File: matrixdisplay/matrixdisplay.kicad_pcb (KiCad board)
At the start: 2 copper layers, 73 x 31 mm, 93 parts, among them J1 FILAS, J2 COLUMNAS, J3 SWD, J4 USART, J5 FILAS, J6 COL, SW1 BT1, SW2 BT2, SW2 P_ON, U1 STM32F051K8Ux

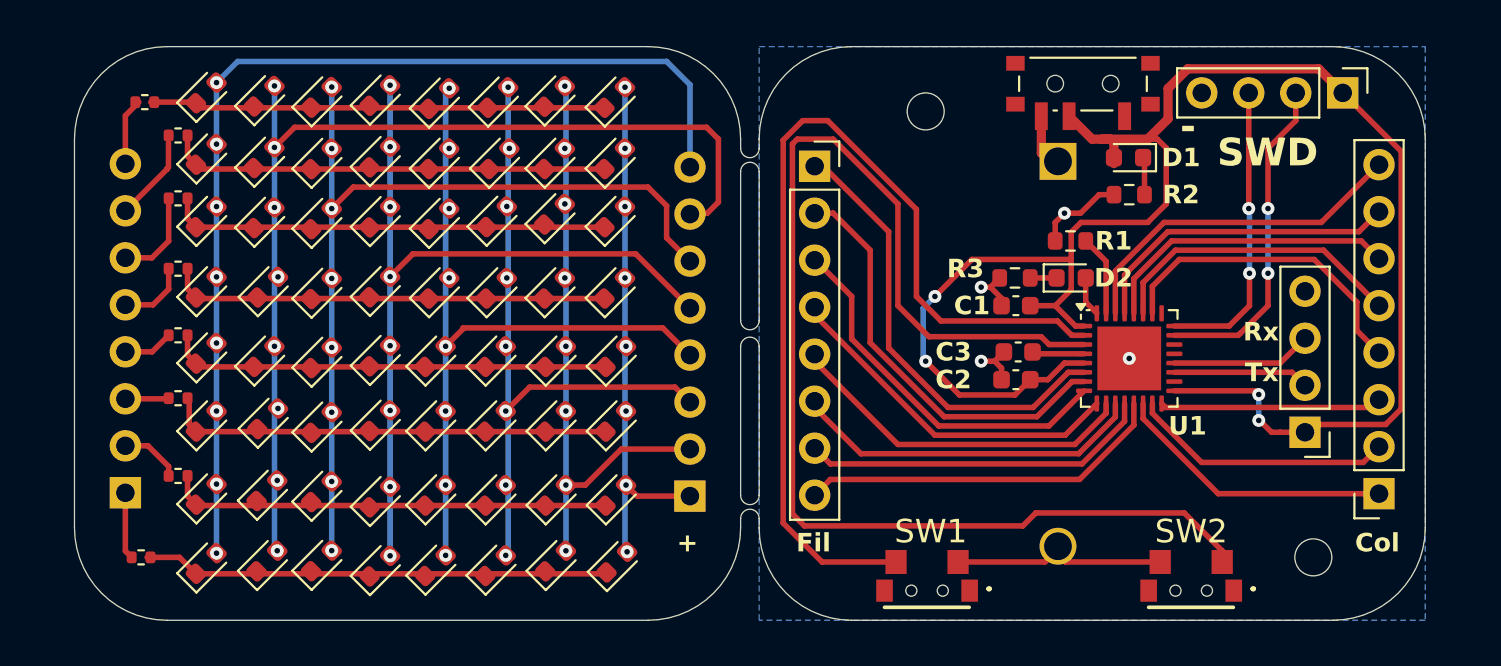
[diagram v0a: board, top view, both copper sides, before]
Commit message: feat(brd): reroute for CR2450
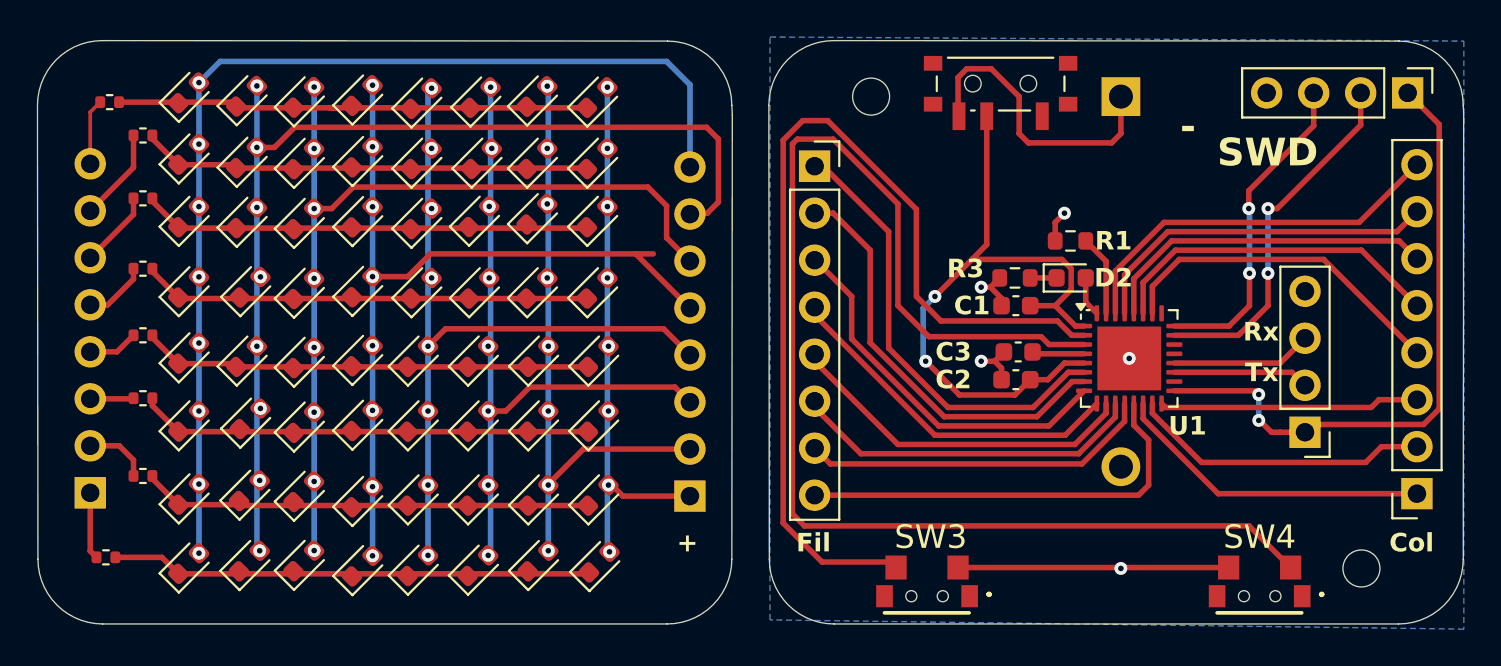
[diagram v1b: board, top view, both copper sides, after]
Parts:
- removed D1: LED, LED_SMD:LED_0603_1608Metric
- removed R2: 220, Resistor_SMD:R_0603_1608Metric
- BT1: value CR2032 -> CR2450; footprint Battery:BatteryHolder_MYOUNG_BS-07-A1BJ001_CR2032 -> Battery:BatteryHolder_ComfortableElectronic_CH273-2450_1x2450
- moved BT1 4.88 mm to (173.0, 77.5)
- moved SW2 4.45 mm to (166.5, 77.1)
- moved SW4 3.71 mm to (180.5, 104.5)
- moved J3 3.51 mm to (188.5, 77.3)
- moved H1 3.06 mm to (159.5, 77.5)
- moved H2 2.67 mm to (186.0, 103.0)
- moved J2 2.05 mm to (189.0, 99.0)
- moved J6 1.90 mm to (117.3, 98.9)
- moved R11 1.90 mm to (118.3, 77.8)
- moved R10 1.90 mm to (120.2, 79.6)
- moved R4 1.90 mm to (118.2, 102.4)
- moved R5 1.90 mm to (120.2, 98.0)
- moved R6 1.90 mm to (120.2, 93.8)
- moved R7 1.90 mm to (120.2, 90.4)
- moved R8 1.90 mm to (120.2, 86.8)
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- renumbered SW1 to SW3, SW2 to SW4
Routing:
- net +3.3V: track 93.4 -> 70.4 mm
- net Net-(BT1-+): track 3.05 -> 16.1 mm
- net Net-(J1-Pin_8): track 20.0 -> 23.0 mm
- net Net-(U1-PF1): track 68.9 -> 71.8 mm
- net Net-(J2-Pin_5): track 16.4 -> 18.4 mm
- net Net-(J2-Pin_3): track 12.0 -> 14.1 mm
- net Net-(J2-Pin_1): track 15.2 -> 17.3 mm
- net Net-(J2-Pin_8): track 18.9 -> 21.0 mm
- net Net-(J2-Pin_7): track 17.2 -> 19.3 mm
- net Net-(J2-Pin_6): track 16.4 -> 18.4 mm
- net Net-(J2-Pin_2): track 14.2 -> 16.3 mm
- net Net-(D1-K): track 2.03 -> 0.00 mm
- net Net-(D27-A): track 43.6 -> 45.5 mm
- net Net-(J3-Pin_2): track 17.8 -> 19.6 mm
- net Net-(J3-Pin_3): track 16.0 -> 17.5 mm
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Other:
- board size 73 x 31 mm -> 77.1 x 31.5 mm

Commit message: Fix (brd): DRC errors
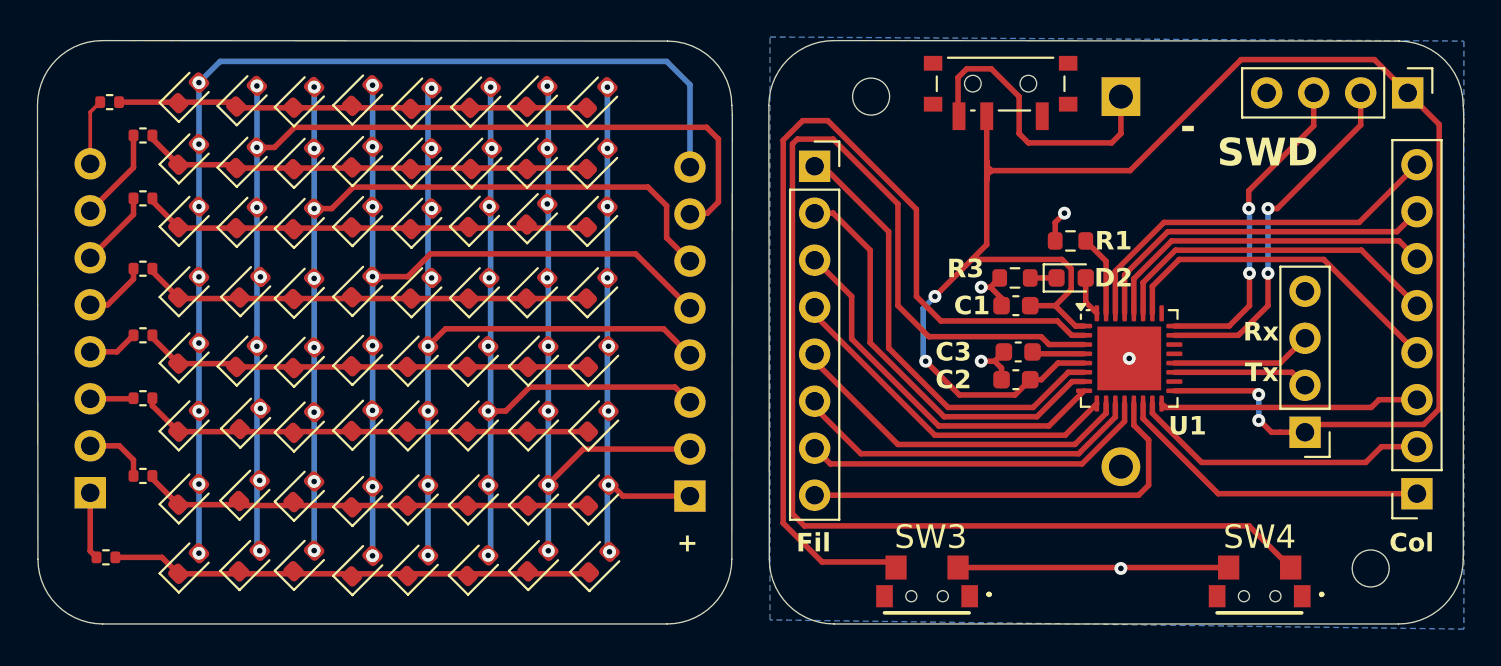
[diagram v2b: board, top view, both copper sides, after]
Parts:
- moved H2 0.50 mm to (186.5, 103.0)
- renumbered BT1 to +
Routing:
- net +3.3V: track 70.4 -> 97.6 mm
- net Net-(D27-A): track 45.5 -> 44.5 mm
- net GND: track 22.0 -> 21.4 mm
- net Net-(D11-K): track 25.9 -> 25.4 mm
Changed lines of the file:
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@@
 	(footprint "MountingHole:MountingHole_2mm"
 		(layer "F.Cu")
-		(at 186 103)
+		(at 186.5 103)
 		(descr "Mounting Hole 2mm, no annular")
 		(tags "mounting hole 2mm no annular")
@@
 		(descr "Comfortable Electronic CR2450 battery holder, http://www.comf.com.tw/ProductDetail.asp?no=148")
 		(tags "Comfortable Electronic CR2450")
-		(property "Reference" "BT1"
+		(property "Reference" "+"
 			(at 0.1 6.62 90)
 			(layer "B.SilkS")
@@
 				(font
 					(size 1 1)
-					(thickness 0.15)
+					(thickness 0.2)
+					(bold yes)
 				)
 				(justify mirror)
@@
 	)
 	(gr_text "ArcMaker\n${VERSION}"
-		(at 161.5 82.5 0)
+		(at 184.25 82 0)
 		(layer "B.SilkS")
 		(effects
 			(font
-				(size 0.75 1)
-				(thickness 0.1875)
+				(size 1 1)
+				(thickness 0.2)
 				(bold yes)
 			)
@@
 	)
 	(segment
-		(start 178.976 102.857521)
-		(end 178.976 102.65)
-		(width 0.3)
-		(layer "F.Cu")
-		(net 1)
-	)
-	(segment
 		(start 165.95 87.8)
 		(end 166.45 87.3)
@@
 	)
 	(segment
-		(start 178.682521 103.151)
-		(end 178.976 102.857521)
-		(width 0.3)
-		(layer "F.Cu")
-		(net 1)
-	)
-	(segment
 		(start 169.45 85.3)
 		(end 169.45 84.3)
@@
 	)
 	(segment
+		(start 165.75 81.25)
+		(end 166 81.5)
+		(width 0.3)
+		(layer "F.Cu")
+		(net 3)
+	)
+	(segment
 		(start 165.75 78.56)
-		(end 165.75 85.5)
+		(end 165.75 81)
 		(width 0.3)
 		(layer "F.Cu")
@@
 	)
 	(segment
-		(start 175.8875 93.4)
-		(end 180.25 93.4)
+		(start 180.25 93.4)
+		(end 180.45 93.6)
 		(width 0.3)
 		(layer "F.Cu")
@@
 	)
 	(segment
-		(start 180.25 93.4)
-		(end 180.45 93.6)
+		(start 165.75 81)
+		(end 165.75 81.5)
 		(width 0.3)
 		(layer "F.Cu")
@@
 	)
 	(segment
+		(start 165.75 81.75)
+		(end 166 81.5)
+		(width 0.3)
+		(layer "F.Cu")
+		(net 3)
+	)
+	(segment
 		(start 164.95 86.3)
 		(end 165.75 85.5)
@@
 	)
 	(segment
-		(start 169.05 92.8)
-		(end 169.95 91.9)
+		(start 179.5 75.5)
+		(end 173.5 81.5)
+		(width 0.3)
+		(layer "F.Cu")
+		(net 3)
+	)
+	(segment
+		(start 173.5 81.5)
+		(end 166 81.5)
 		(width 0.3)
 		(layer "F.Cu")
@@
 	)
 	(segment
-		(start 169.95 91.9)
-		(end 171.0125 91.9)
+		(start 188.5 77.3)
+		(end 186.7 75.5)
 		(width 0.3)
 		(layer "F.Cu")
@@
 	)
 	(segment
+		(start 165.75 82)
+		(end 165.75 81.75)
+		(width 0.3)
+		(layer "F.Cu")
+		(net 3)
+	)
+	(segment
+		(start 169.6 91.9)
+		(end 168.7 92.8)
+		(width 0.3)
+		(layer "F.Cu")
+		(net 3)
+	)
+	(segment
 		(start 162.95 88.3)
 		(end 164.95 86.3)
@@
 	)
 	(segment
+		(start 165.75 82)
+		(end 165.75 85.5)
+		(width 0.3)
+		(layer "F.Cu")
+		(net 3)
+	)
+	(segment
 		(start 180.45 94.95)
 		(end 181.14 95.64)
@@
 	)
 	(segment
+		(start 171.0125 91.9)
+		(end 169.6 91.9)
+		(width 0.3)
+		(layer "F.Cu")
+		(net 3)
+	)
+	(segment
+		(start 165.75 81.5)
+		(end 165.75 82)
+		(width 0.3)
+		(layer "F.Cu")
+		(net 3)
+	)
+	(segment
 		(start 190.201 79.001)
 		(end 188.5 77.3)
@@
 	)
 	(segment
+		(start 168.7 92.8)
+		(end 168.1 92.8)
+		(width 0.3)
+		(layer "F.Cu")
+		(net 3)
+	)
+	(segment
 		(start 181.61 95.64)
 		(end 182.95 95.64)
@@
 	)
 	(segment
+		(start 175.8875 93.4)
+		(end 180.25 93.4)
+		(width 0.3)
+		(layer "F.Cu")
+		(net 3)
+	)
+	(segment
+		(start 186.7 75.5)
+		(end 179.5 75.5)
+		(width 0.3)
+		(layer "F.Cu")
+		(net 3)
+	)
+	(segment
 		(start 167.275 93.625)
 		(end 164.275 93.625)
@@
 	)
 	(segment
+		(start 166 81.5)
+		(end 165.75 81.5)
+		(width 0.3)
+		(layer "F.Cu")
+		(net 3)
+	)
+	(segment
 		(start 190.201 94.377471)
 		(end 190.201 79.001)
@@
 	)
 	(segment
-		(start 168.1 92.8)
-		(end 169.05 92.8)
+		(start 165.75 81)
+		(end 165.75 81.25)
 		(width 0.3)
 		(layer "F.Cu")
@@
 	)
 	(segment
-		(start 180.45 93.6)
-		(end 180.45 95)
-		(width 0.3)
-		(layer "B.Cu")
-		(net 3)
-	)
-	(segment
 		(start 162.316835 88.933165)
 		(end 162.95 88.3)
@@
 	)
 	(segment
+		(start 180.45 95)
+		(end 180.45 93.6)
+		(width 0.3)
+		(layer "B.Cu")
+		(net 3)
+	)
+	(segment
 		(start 168.225 91.3)
 		(end 168.325 91.4)
@@
 	)
 	(segment
-		(start 171.1 88.6125)
-		(end 171.7 89.2125)
+		(start 171.1 87.3)
+		(end 171.1 88.6125)
 		(width 0.3)
 		(layer "F.Cu")
@@
 	)
 	(segment
-		(start 171.1 87.3)
-		(end 171.1 88.6125)
+		(start 171.1 88.6125)
+		(end 171.7 89.2125)
 		(width 0.3)
 		(layer "F.Cu")
@@
 	)
 	(segment
-		(start 130.188153 78.096847)
-		(end 130.6975 78.096847)
-		(width 0.3)
-		(layer "F.Cu")
-		(net 34)
-	)
-	(segment
 		(start 120.66 79.778694)
 		(end 122.063153 81.181847)
@@
 	)
 	(segment
-		(start 132.5575 87.23)
-		(end 134.4575 87.23)
+		(start 146.780652 86)
+		(end 135.6875 86)
 		(width 0.3)
 		(layer "F.Cu")
@@
 	(segment
 		(start 134.4575 87.23)
-		(end 135.6875 86)
+		(end 132.5575 87.23)
 		(width 0.3)
 		(layer "F.Cu")
@@
 	)
 	(segment
-		(start 147.731306 86)
-		(end 135.6875 86)
+		(start 135.6875 86)
+		(end 134.4575 87.23)
 		(width 0.3)
 		(layer "F.Cu")
